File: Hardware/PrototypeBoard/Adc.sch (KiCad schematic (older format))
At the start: 30 parts, among them U5 ADC124S021

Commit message: All tracks routed, fixed bug in schematic, smaller test points
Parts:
- TP22, TP23, TP24, TP25, TP26, TP27, TP28, TP29, TP30: footprint Pin_Headers:Pin_Header_Straight_1x01_Pitch2.00mm -> Pin_Headers:Pin_Header_Straight_1x01_Pitch1.00mm
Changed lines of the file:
@@
 F 0 "TP27" H 5100 4200 50  0000 C BNN
 F 1 "Adc4" H 5100 4150 50  0000 C CNN
-F 2 "Pin_Headers:Pin_Header_Straight_1x01_Pitch2.00mm" H 5100 3900 50  0001 C CNN
+F 2 "Pin_Headers:Pin_Header_Straight_1x01_Pitch1.00mm" H 5100 3900 50  0001 C CNN
 F 3 "" H 5100 3900 50  0001 C CNN
 	1    5100 3900
@@
 F 0 "TP28" H 6500 4200 50  0000 C BNN
 F 1 "Adc3" H 6500 4150 50  0000 C CNN
-F 2 "Pin_Headers:Pin_Header_Straight_1x01_Pitch2.00mm" H 6500 3900 50  0001 C CNN
+F 2 "Pin_Headers:Pin_Header_Straight_1x01_Pitch1.00mm" H 6500 3900 50  0001 C CNN
 F 3 "" H 6500 3900 50  0001 C CNN
 	1    6500 3900
@@
 F 0 "TP29" H 7900 4200 50  0000 C BNN
 F 1 "Adc2" H 7900 4150 50  0000 C CNN
-F 2 "Pin_Headers:Pin_Header_Straight_1x01_Pitch2.00mm" H 7900 3900 50  0001 C CNN
+F 2 "Pin_Headers:Pin_Header_Straight_1x01_Pitch1.00mm" H 7900 3900 50  0001 C CNN
 F 3 "" H 7900 3900 50  0001 C CNN
 	1    7900 3900
@@
 F 0 "TP30" H 9300 4200 50  0000 C BNN
 F 1 "Adc1" H 9300 4150 50  0000 C CNN
-F 2 "Pin_Headers:Pin_Header_Straight_1x01_Pitch2.00mm" H 9300 3900 50  0001 C CNN
+F 2 "Pin_Headers:Pin_Header_Straight_1x01_Pitch1.00mm" H 9300 3900 50  0001 C CNN
 F 3 "" H 9300 3900 50  0001 C CNN
 	1    9300 3900
@@
 F 0 "TP25" H 2800 3400 50  0000 C BNN
 F 1 "AdcV" H 2800 3350 50  0000 C CNN
-F 2 "Pin_Headers:Pin_Header_Straight_1x01_Pitch2.00mm" H 2800 3100 50  0001 C CNN
+F 2 "Pin_Headers:Pin_Header_Straight_1x01_Pitch1.00mm" H 2800 3100 50  0001 C CNN
 F 3 "" H 2800 3100 50  0001 C CNN
 	1    2800 3100
@@
 F 0 "TP26" H 2950 4100 50  0000 C BNN
 F 1 "~AdcCs" H 2950 4050 50  0000 C CNN
-F 2 "Pin_Headers:Pin_Header_Straight_1x01_Pitch2.00mm" H 2950 3800 50  0001 C CNN
+F 2 "Pin_Headers:Pin_Header_Straight_1x01_Pitch1.00mm" H 2950 3800 50  0001 C CNN
 F 3 "" H 2950 3800 50  0001 C CNN
 	1    2950 3800
@@
 F 0 "TP24" H 2700 4100 50  0000 C BNN
 F 1 "AdcSclk" H 2700 4050 50  0000 C CNN
-F 2 "Pin_Headers:Pin_Header_Straight_1x01_Pitch2.00mm" H 2700 3800 50  0001 C CNN
+F 2 "Pin_Headers:Pin_Header_Straight_1x01_Pitch1.00mm" H 2700 3800 50  0001 C CNN
 F 3 "" H 2700 3800 50  0001 C CNN
 	1    2700 3800
@@
 F 0 "TP23" H 2450 4100 50  0000 C BNN
 F 1 "AdcMosi" H 2450 4050 50  0000 C CNN
-F 2 "Pin_Headers:Pin_Header_Straight_1x01_Pitch2.00mm" H 2450 3800 50  0001 C CNN
+F 2 "Pin_Headers:Pin_Header_Straight_1x01_Pitch1.00mm" H 2450 3800 50  0001 C CNN
 F 3 "" H 2450 3800 50  0001 C CNN
 	1    2450 3800
@@
 F 0 "TP22" H 2200 4100 50  0000 C BNN
 F 1 "AdcMiso" H 2200 4050 50  0000 C CNN
-F 2 "Pin_Headers:Pin_Header_Straight_1x01_Pitch2.00mm" H 2200 3800 50  0001 C CNN
+F 2 "Pin_Headers:Pin_Header_Straight_1x01_Pitch1.00mm" H 2200 3800 50  0001 C CNN
 F 3 "" H 2200 3800 50  0001 C CNN
 	1    2200 3800

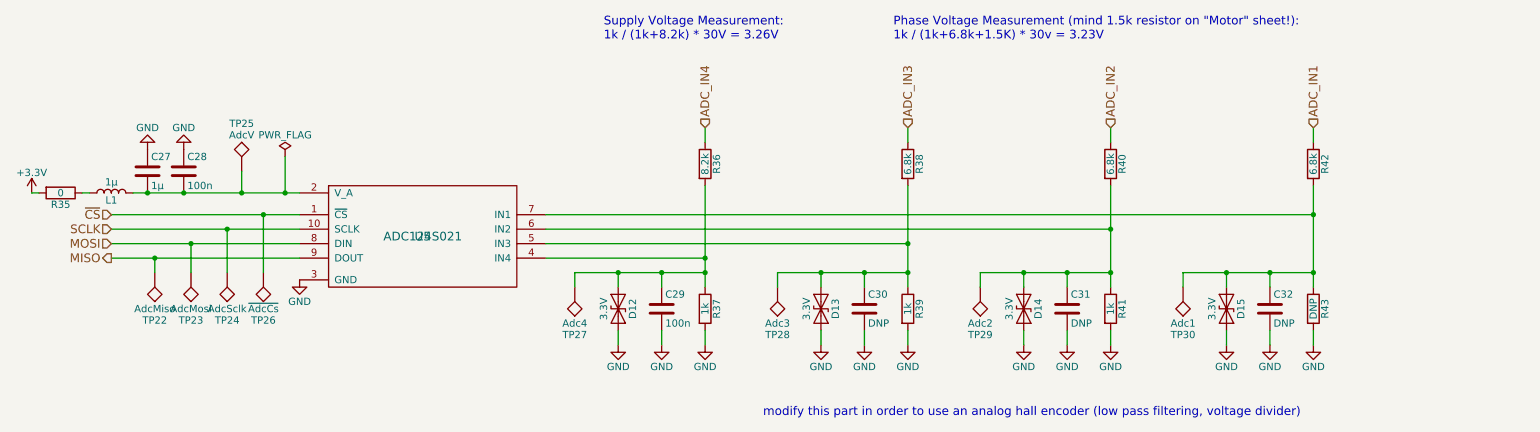
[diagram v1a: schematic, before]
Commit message: Some deduplication, renaming and cleanups in the schematic
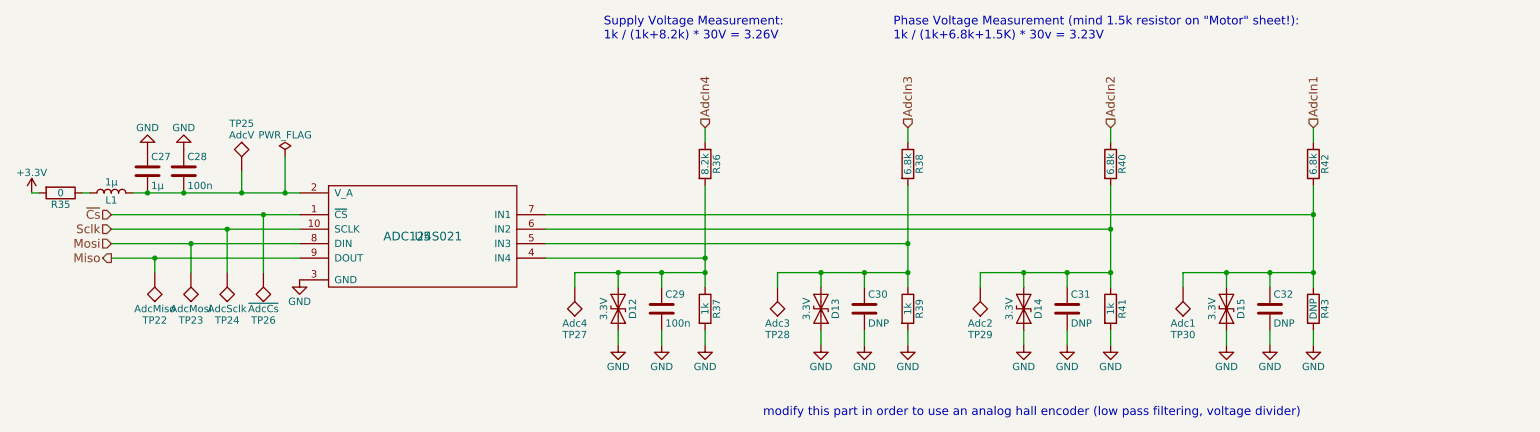
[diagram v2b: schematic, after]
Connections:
- net ADC_IN1 renamed AdcIn1
- net ADC_IN2 renamed AdcIn2
- net ADC_IN3 renamed AdcIn3
- net ADC_IN4 renamed AdcIn4
- net MISO renamed Miso
- net MOSI renamed Mosi
- net SCLK renamed Sclk
- net ~CS renamed ~Cs
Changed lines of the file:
@@
 $Descr A4 11693 8268
 encoding utf-8
-Sheet 6 8
+Sheet 6 13
 Title ""
 Date ""
@@
 $EndComp
 Text HLabel 10200 2800 1    60   Input ~ 0
-ADC_IN1
+AdcIn1
 Text HLabel 8800 2800 1    60   Input ~ 0
-ADC_IN2
+AdcIn2
 Text HLabel 7400 2800 1    60   Input ~ 0
-ADC_IN3
+AdcIn3
 Text HLabel 6000 2800 1    60   Input ~ 0
-ADC_IN4
+AdcIn4
 $Comp
 L Device:L L1
@@
 $EndComp
 Text HLabel 1900 3400 0    60   Input ~ 0
-~CS
+~Cs
 Text HLabel 1900 3500 0    60   Input ~ 0
-SCLK
+Sclk
 Text HLabel 1900 3600 0    60   Input ~ 0
-MOSI
+Mosi
 Text HLabel 1900 3700 0    60   Output ~ 0
-MISO
-Wire Wire Line
-	2050 3250 3200 3250
+Miso
+Wire Wire Line
+	2050 3250 2150 3250
 Connection ~ 2150 3250
 Connection ~ 2400 3250
@@
 $EndComp
 Wire Wire Line
-	1900 3400 3200 3400
-Wire Wire Line
-	1900 3500 3200 3500
-Wire Wire Line
-	1900 3600 3200 3600
-Wire Wire Line
-	1900 3700 3200 3700
+	1900 3400 2950 3400
+Wire Wire Line
+	1900 3500 2700 3500
+Wire Wire Line
+	1900 3600 2450 3600
+Wire Wire Line
+	1900 3700 2200 3700
 $Comp
 L Device:C C32
@@
 	4900 3700 6000 3700
 Wire Wire Line
-	5100 3800 6000 3800
-Wire Wire Line
-	6500 3800 7400 3800
-Wire Wire Line
-	7900 3800 8800 3800
-Wire Wire Line
-	9300 3800 10200 3800
+	5100 3800 5400 3800
+Wire Wire Line
+	6500 3800 6800 3800
+Wire Wire Line
+	7900 3800 8200 3800
+Wire Wire Line
+	9300 3800 9600 3800
 Wire Wire Line
 	5100 3800 5100 3900
@@
 Connection ~ 5700 3800
 Wire Wire Line
-	6000 3200 6000 3900
+	6000 3200 6000 3700
 Wire Wire Line
 	6500 3900 6500 3800
@@
 Connection ~ 7100 3800
 Wire Wire Line
-	7400 3200 7400 3900
+	7400 3200 7400 3600
 Wire Wire Line
 	7900 3900 7900 3800
@@
 Connection ~ 8500 3800
 Wire Wire Line
-	8800 3200 8800 3900
+	8800 3200 8800 3500
 Wire Wire Line
 	9300 3900 9300 3800
@@
 Connection ~ 9900 3800
 Wire Wire Line
-	10200 3200 10200 3900
+	10200 3200 10200 3400
 $Comp
 L power:GND #PWR060
@@
 Wire Wire Line
 	1700 3250 1750 3250
+Wire Wire Line
+	2150 3250 2400 3250
+Wire Wire Line
+	2400 3250 2800 3250
+Wire Wire Line
+	2200 3700 3200 3700
+Wire Wire Line
+	2450 3600 3200 3600
+Wire Wire Line
+	2700 3500 3200 3500
+Wire Wire Line
+	2950 3400 3200 3400
+Wire Wire Line
+	2800 3250 3100 3250
+Wire Wire Line
+	3100 3250 3200 3250
+Wire Wire Line
+	5400 3800 5700 3800
+Wire Wire Line
+	5700 3800 6000 3800
+Wire Wire Line
+	6800 3800 7100 3800
+Wire Wire Line
+	7100 3800 7400 3800
+Wire Wire Line
+	8200 3800 8500 3800
+Wire Wire Line
+	8500 3800 8800 3800
+Wire Wire Line
+	9600 3800 9900 3800
+Wire Wire Line
+	9900 3800 10200 3800
+Wire Wire Line
+	6000 3800 6000 3900
+Wire Wire Line
+	7400 3800 7400 3900
+Wire Wire Line
+	8800 3800 8800 3900
+Wire Wire Line
+	10200 3800 10200 3900
+Wire Wire Line
+	10200 3400 10200 3800
+Wire Wire Line
+	8800 3500 8800 3800
+Wire Wire Line
+	7400 3600 7400 3800
+Wire Wire Line
+	6000 3700 6000 3800
 $EndSCHEMATC
